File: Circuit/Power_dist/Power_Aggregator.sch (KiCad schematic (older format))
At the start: 8 parts, among them P16 XT60, P17 XT60, Q6 AUIRFS8409-7P, Q7 AUIRFS8409-7P, U5 LTC4357, U6 LTC4357

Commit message: edit sch and add pcix16
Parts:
- F6, F7: footprint Zeabus:FUSE_AUTO -> zeabus:FUSE_AUTO
- P16, P17: footprint Zeabus:XT60 -> zeabus:XT60
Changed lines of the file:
@@
 EESchema Schematic File Version 2
+LIBS:Power_Distributor-rescue
 LIBS:power
 LIBS:device
@@
 LIBS:zeabus
 LIBS:ftdi
+LIBS:Power_Distributor-cache
 EELAYER 25 0
 EELAYER END
@@
 F 0 "F7" H 4400 4050 50  0000 C CNN
 F 1 "FUSE" H 4200 3950 50  0000 C CNN
-F 2 "Zeabus:FUSE_AUTO" H 4300 4000 60  0001 C CNN
+F 2 "zeabus:FUSE_AUTO" H 4300 4000 60  0001 C CNN
 F 3 "" H 4300 4000 60  0000 C CNN
 	1    4300 4000
@@
 F 0 "P17" H 3850 4600 50  0000 C CNN
 F 1 "XT60" H 3850 4300 50  0000 C CNN
-F 2 "Zeabus:XT60" H 3850 4450 60  0001 C CNN
+F 2 "zeabus:XT60" H 3850 4450 60  0001 C CNN
 F 3 "" H 3850 4450 60  0000 C CNN
 	1    3850 4450
@@
 $EndComp
 $Comp
-L GND #PWR040
+L GND #PWR025
 U 1 1 5626F752
 P 6350 5250
-F 0 "#PWR040" H 6350 5000 50  0001 C CNN
+F 0 "#PWR025" H 6350 5000 50  0001 C CNN
 F 1 "GND" H 6350 5100 50  0000 C CNN
 F 2 "" H 6350 5250 60  0000 C CNN
@@
 $EndComp
 $Comp
-L GND #PWR041
+L GND #PWR026
 U 1 1 5626F76E
 P 4050 4600
-F 0 "#PWR041" H 4050 4350 50  0001 C CNN
+F 0 "#PWR026" H 4050 4350 50  0001 C CNN
 F 1 "GND" H 4050 4450 50  0000 C CNN
 F 2 "" H 4050 4600 60  0000 C CNN
@@
 F 0 "F6" H 4400 2150 50  0000 C CNN
 F 1 "FUSE" H 4200 2050 50  0000 C CNN
-F 2 "Zeabus:FUSE_AUTO" H 4300 2100 60  0001 C CNN
+F 2 "zeabus:FUSE_AUTO" H 4300 2100 60  0001 C CNN
 F 3 "" H 4300 2100 60  0000 C CNN
 	1    4300 2100
@@
 F 0 "P16" H 3850 2700 50  0000 C CNN
 F 1 "XT60" H 3850 2400 50  0000 C CNN
-F 2 "Zeabus:XT60" H 3850 2550 60  0001 C CNN
+F 2 "zeabus:XT60" H 3850 2550 60  0001 C CNN
 F 3 "" H 3850 2550 60  0000 C CNN
 	1    3850 2550
@@
 $EndComp
 $Comp
-L GND #PWR042
+L GND #PWR027
 U 1 1 5626F959
 P 6350 3350
-F 0 "#PWR042" H 6350 3100 50  0001 C CNN
+F 0 "#PWR027" H 6350 3100 50  0001 C CNN
 F 1 "GND" H 6350 3200 50  0000 C CNN
 F 2 "" H 6350 3350 60  0000 C CNN
@@
 $EndComp
 $Comp
-L GND #PWR043
+L GND #PWR028
 U 1 1 5626F95F
 P 4050 2700
-F 0 "#PWR043" H 4050 2450 50  0001 C CNN
+F 0 "#PWR028" H 4050 2450 50  0001 C CNN
 F 1 "GND" H 4050 2550 50  0000 C CNN
 F 2 "" H 4050 2700 60  0000 C CNN

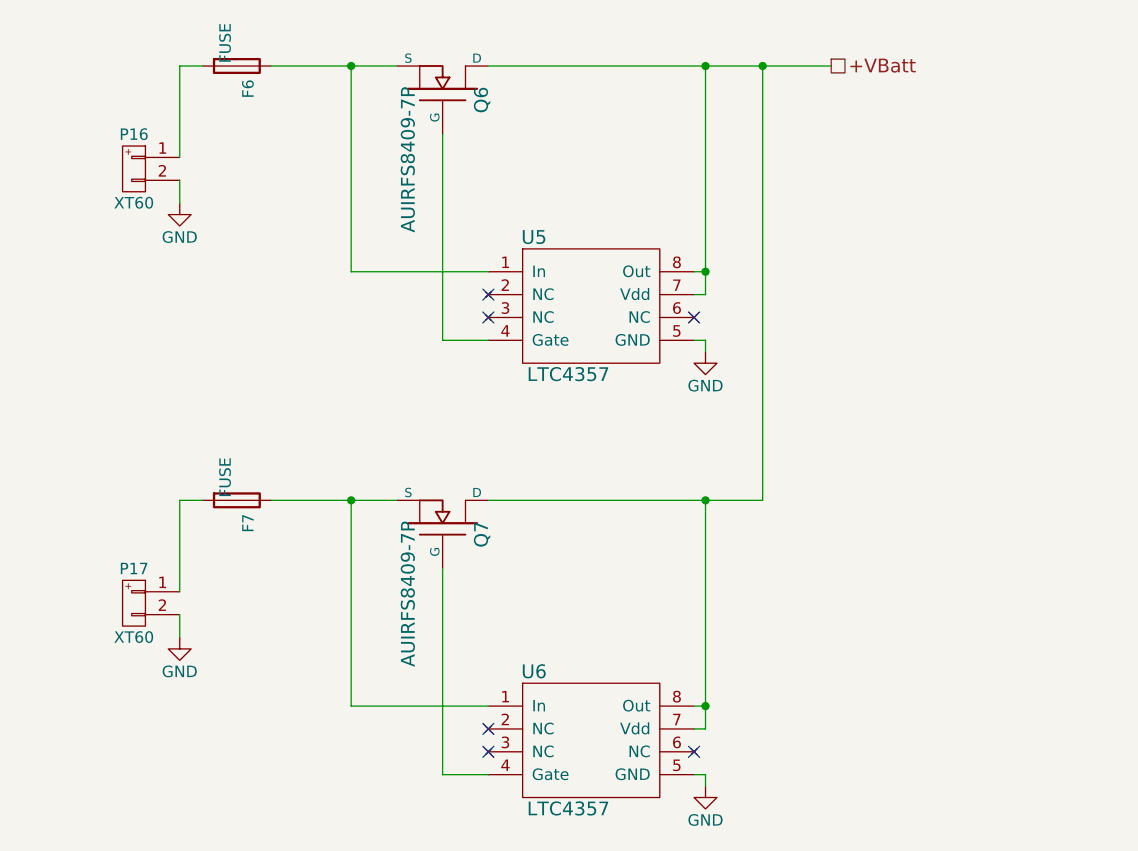
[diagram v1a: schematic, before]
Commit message: delete fuses at thrusters and oring + add power on jumper
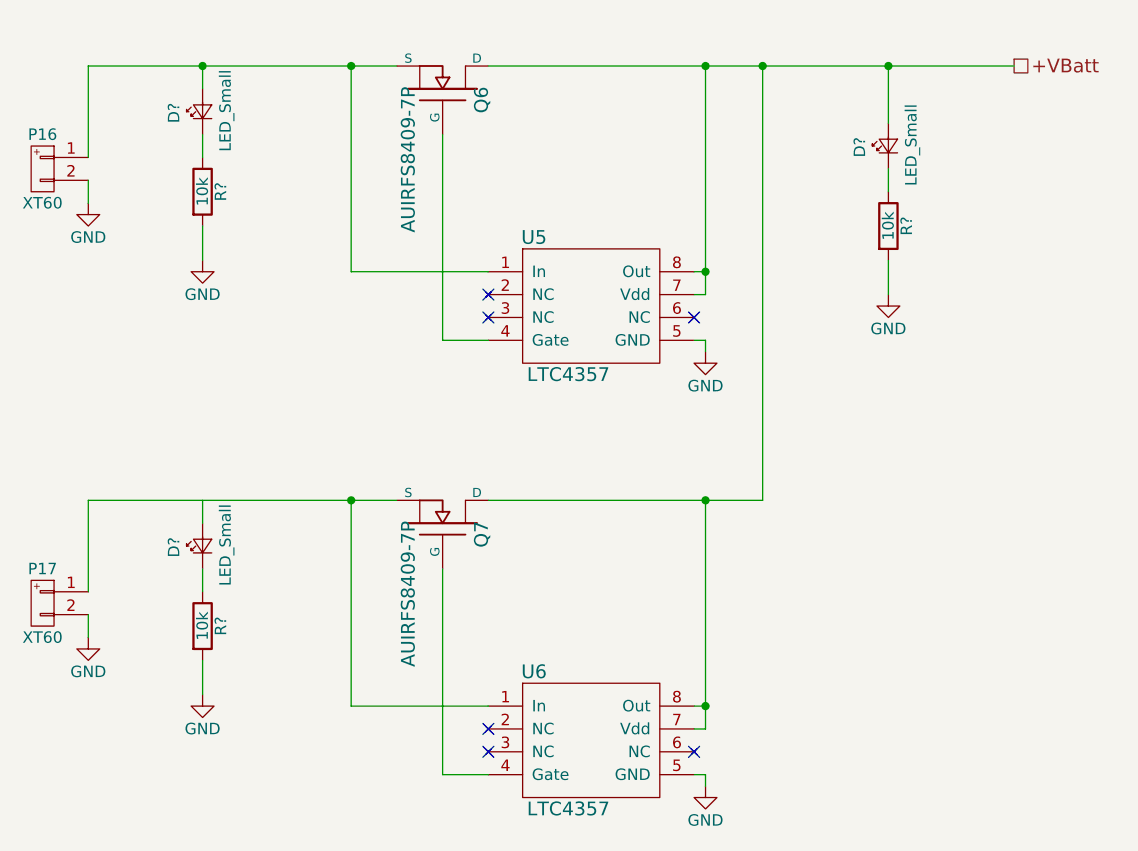
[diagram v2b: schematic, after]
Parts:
- removed F6, F7: FUSE, zeabus:FUSE_AUTO, symbol Fuse
- added D? (x3): LED_Small, LEDs:LED_0603, symbol LED_Small
- added R? (x3): 10k, Resistors_SMD:R_0603, symbol R
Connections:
- net +VBatt: now also D?.2 (A)
- net GND: now also R?.2, R?.2, R?.2
- net at Q7.S, U6.1 (In): now also P17.1 (P1)
- net at Q6.S, U5.1 (In): now also P16.1 (P1), D?.2 (A)
- new net: D?.1 (K), R?.1 (x3)
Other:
- moved on the sheet: P16, P17
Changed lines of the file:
@@
 $Descr A4 11693 8268
 encoding utf-8
-Sheet 8 9
+Sheet 6 8
 Title "Power Aggregator"
 Date "2017-04-06"
@@
 $EndDescr
 $Comp
-L Fuse F7
-U 1 1 5626464E
-P 4300 4000
-F 0 "F7" H 4400 4050 50  0000 C CNN
-F 1 "FUSE" H 4200 3950 50  0000 C CNN
-F 2 "zeabus:FUSE_AUTO" H 4300 4000 60  0001 C CNN
-F 3 "" H 4300 4000 60  0000 C CNN
-	1    4300 4000
-	0    1    1    0
-$EndComp
-$Comp
 L XT60 P17
 U 1 1 5626F4F4
-P 3850 4450
-F 0 "P17" H 3850 4600 50  0000 C CNN
-F 1 "XT60" H 3850 4300 50  0000 C CNN
-F 2 "zeabus:XT60" H 3850 4450 60  0001 C CNN
-F 3 "" H 3850 4450 60  0000 C CNN
-	1    3850 4450
+P 3450 4450
+F 0 "P17" H 3450 4600 50  0000 C CNN
+F 1 "XT60" H 3450 4300 50  0000 C CNN
+F 2 "zeabus:XT60" H 3450 4450 60  0001 C CNN
+F 3 "" H 3450 4450 60  0000 C CNN
+	1    3450 4450
 	-1   0    0    -1
 $EndComp
@@
 L GND #PWR026
 U 1 1 5626F76E
-P 4050 4600
-F 0 "#PWR026" H 4050 4350 50  0001 C CNN
-F 1 "GND" H 4050 4450 50  0000 C CNN
-F 2 "" H 4050 4600 60  0000 C CNN
-F 3 "" H 4050 4600 60  0000 C CNN
-	1    4050 4600
-	1    0    0    -1
-$EndComp
-Wire Wire Line
-	4050 4400 4050 4000
-Wire Wire Line
-	4450 4000 5000 4000
+P 3650 4600
+F 0 "#PWR026" H 3650 4350 50  0001 C CNN
+F 1 "GND" H 3650 4450 50  0000 C CNN
+F 2 "" H 3650 4600 60  0000 C CNN
+F 3 "" H 3650 4600 60  0000 C CNN
+	1    3650 4600
+	1    0    0    -1
+$EndComp
+Wire Wire Line
+	3650 4400 3650 4000
+Wire Wire Line
+	3650 4000 5000 4000
 Wire Wire Line
 	5400 5200 5200 5200
@@
 	6350 5200 6300 5200
 Wire Wire Line
-	4050 4500 4050 4600
-$Comp
-L Fuse F6
-U 1 1 5626F941
-P 4300 2100
-F 0 "F6" H 4400 2150 50  0000 C CNN
-F 1 "FUSE" H 4200 2050 50  0000 C CNN
-F 2 "zeabus:FUSE_AUTO" H 4300 2100 60  0001 C CNN
-F 3 "" H 4300 2100 60  0000 C CNN
-	1    4300 2100
-	0    1    1    0
-$EndComp
+	3650 4500 3650 4600
 $Comp
 L XT60 P16
 U 1 1 5626F947
-P 3850 2550
-F 0 "P16" H 3850 2700 50  0000 C CNN
-F 1 "XT60" H 3850 2400 50  0000 C CNN
-F 2 "zeabus:XT60" H 3850 2550 60  0001 C CNN
-F 3 "" H 3850 2550 60  0000 C CNN
-	1    3850 2550
+P 3450 2550
+F 0 "P16" H 3450 2700 50  0000 C CNN
+F 1 "XT60" H 3450 2400 50  0000 C CNN
+F 2 "zeabus:XT60" H 3450 2550 60  0001 C CNN
+F 3 "" H 3450 2550 60  0000 C CNN
+	1    3450 2550
 	-1   0    0    -1
 $EndComp
@@
 L GND #PWR028
 U 1 1 5626F95F
-P 4050 2700
-F 0 "#PWR028" H 4050 2450 50  0001 C CNN
-F 1 "GND" H 4050 2550 50  0000 C CNN
-F 2 "" H 4050 2700 60  0000 C CNN
-F 3 "" H 4050 2700 60  0000 C CNN
-	1    4050 2700
-	1    0    0    -1
-$EndComp
-Wire Wire Line
-	4050 2500 4050 2100
-Wire Wire Line
-	4450 2100 5000 2100
+P 3650 2700
+F 0 "#PWR028" H 3650 2450 50  0001 C CNN
+F 1 "GND" H 3650 2550 50  0000 C CNN
+F 2 "" H 3650 2700 60  0000 C CNN
+F 3 "" H 3650 2700 60  0000 C CNN
+	1    3650 2700
+	1    0    0    -1
+$EndComp
+Wire Wire Line
+	3650 2500 3650 2100
+Wire Wire Line
+	3650 2100 5000 2100
 Wire Wire Line
 	5400 3300 5200 3300
@@
 	6350 3000 6300 3000
 Wire Wire Line
-	5400 2100 6900 2100
+	5400 2100 7700 2100
 Connection ~ 6350 3000
 Wire Wire Line
@@
 	6350 3300 6300 3300
 Wire Wire Line
-	4050 2600 4050 2700
-Text HLabel 6900 2100 2    60   UnSpc ~ 0
+	3650 2600 3650 2700
+Text HLabel 7700 2100 2    60   UnSpc ~ 0
 +VBatt
 Connection ~ 6350 2100
@@
 Connection ~ 6600 2100
 Connection ~ 6350 4000
-Wire Wire Line
-	4050 2100 4150 2100
-Wire Wire Line
-	4050 4000 4150 4000
 NoConn ~ 6300 5100
 NoConn ~ 5400 5000
@@
 NoConn ~ 5400 3200
 NoConn ~ 6300 3200
+$Comp
+L LED_Small D?
+U 1 1 5A394E28
+P 4150 2300
+F 0 "D?" H 4100 2425 50  0000 L CNN
+F 1 "LED_Small" H 3975 2200 50  0000 L CNN
+F 2 "LEDs:LED_0603" V 4150 2300 50  0001 C CNN
+F 3 "" V 4150 2300 50  0001 C CNN
+	1    4150 2300
+	0    -1   -1   0
+$EndComp
+$Comp
+L R R?
+U 1 1 5A394EA7
+P 4150 2650
+F 0 "R?" V 4230 2650 50  0000 C CNN
+F 1 "10k" V 4150 2650 50  0000 C CNN
+F 2 "Resistors_SMD:R_0603" V 4080 2650 50  0001 C CNN
+F 3 "" H 4150 2650 50  0001 C CNN
+	1    4150 2650
+	1    0    0    -1
+$EndComp
+$Comp
+L GND #PWR?
+U 1 1 5A394FC4
+P 4150 2950
+F 0 "#PWR?" H 4150 2700 50  0001 C CNN
+F 1 "GND" H 4150 2800 50  0000 C CNN
+F 2 "" H 4150 2950 60  0000 C CNN
+F 3 "" H 4150 2950 60  0000 C CNN
+	1    4150 2950
+	1    0    0    -1
+$EndComp
+Wire Wire Line
+	4150 2200 4150 2100
+Connection ~ 4150 2100
+Wire Wire Line
+	4150 2400 4150 2500
+Wire Wire Line
+	4150 2800 4150 2950
+$Comp
+L LED_Small D?
+U 1 1 5A3951EC
+P 4150 4200
+F 0 "D?" H 4100 4325 50  0000 L CNN
+F 1 "LED_Small" H 3975 4100 50  0000 L CNN
+F 2 "LEDs:LED_0603" V 4150 4200 50  0001 C CNN
+F 3 "" V 4150 4200 50  0001 C CNN
+	1    4150 4200
+	0    -1   -1   0
+$EndComp
+$Comp
+L R R?
+U 1 1 5A3951F2
+P 4150 4550
+F 0 "R?" V 4230 4550 50  0000 C CNN
+F 1 "10k" V 4150 4550 50  0000 C CNN
+F 2 "Resistors_SMD:R_0603" V 4080 4550 50  0001 C CNN
+F 3 "" H 4150 4550 50  0001 C CNN
+	1    4150 4550
+	1    0    0    -1
+$EndComp
+$Comp
+L GND #PWR?
+U 1 1 5A3951F8
+P 4150 4850
+F 0 "#PWR?" H 4150 4600 50  0001 C CNN
+F 1 "GND" H 4150 4700 50  0000 C CNN
+F 2 "" H 4150 4850 60  0000 C CNN
+F 3 "" H 4150 4850 60  0000 C CNN
+	1    4150 4850
+	1    0    0    -1
+$EndComp
+Wire Wire Line
+	4150 4100 4150 4000
+Wire Wire Line
+	4150 4300 4150 4400
+Wire Wire Line
+	4150 4700 4150 4850
+$Comp
+L LED_Small D?
+U 1 1 5A397232
+P 7150 2450
+F 0 "D?" H 7100 2575 50  0000 L CNN
+F 1 "LED_Small" H 6975 2350 50  0000 L CNN
+F 2 "LEDs:LED_0603" V 7150 2450 50  0001 C CNN
+F 3 "" V 7150 2450 50  0001 C CNN
+	1    7150 2450
+	0    -1   -1   0
+$EndComp
+$Comp
+L R R?
+U 1 1 5A397238
+P 7150 2800
+F 0 "R?" V 7230 2800 50  0000 C CNN
+F 1 "10k" V 7150 2800 50  0000 C CNN
+F 2 "Resistors_SMD:R_0603" V 7080 2800 50  0001 C CNN
+F 3 "" H 7150 2800 50  0001 C CNN
+	1    7150 2800
+	1    0    0    -1
+$EndComp
+$Comp
+L GND #PWR?
+U 1 1 5A39723E
+P 7150 3100
+F 0 "#PWR?" H 7150 2850 50  0001 C CNN
+F 1 "GND" H 7150 2950 50  0000 C CNN
+F 2 "" H 7150 3100 60  0000 C CNN
+F 3 "" H 7150 3100 60  0000 C CNN
+	1    7150 3100
+	1    0    0    -1
+$EndComp
+Wire Wire Line
+	7150 2100 7150 2350
+Wire Wire Line
+	7150 2550 7150 2650
+Wire Wire Line
+	7150 2950 7150 3100
+Connection ~ 7150 2100
 $EndSCHEMATC

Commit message: component alignment on pcb
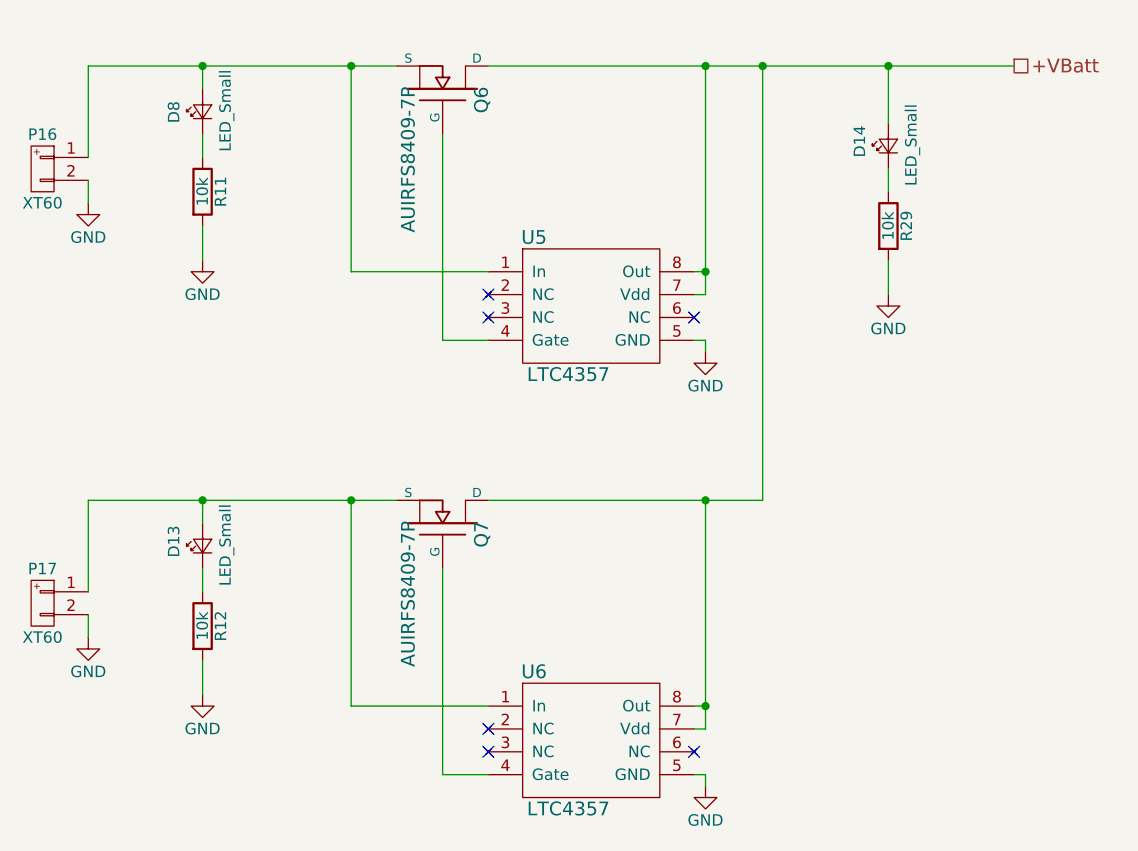
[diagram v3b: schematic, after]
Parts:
- D13, D14, D8: renamed from D?; footprint LEDs:LED_0603 -> LEDs:LED_0603_HandSoldering
- R11, R12, R29: renamed from R?; footprint Resistors_SMD:R_0603 -> Resistors_SMD:R_0603_HandSoldering
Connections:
- net at P17.1 (P1), Q7.S, U6.1 (In): now also D13.2 (A)
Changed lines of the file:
@@
 $EndComp
 $Comp
-L GND #PWR025
+L GND #PWR030
 U 1 1 5626F752
 P 6350 5250
-F 0 "#PWR025" H 6350 5000 50  0001 C CNN
+F 0 "#PWR030" H 6350 5000 50  0001 C CNN
 F 1 "GND" H 6350 5100 50  0000 C CNN
 F 2 "" H 6350 5250 60  0000 C CNN
@@
 $EndComp
 $Comp
-L GND #PWR026
+L GND #PWR031
 U 1 1 5626F76E
 P 3650 4600
-F 0 "#PWR026" H 3650 4350 50  0001 C CNN
+F 0 "#PWR031" H 3650 4350 50  0001 C CNN
 F 1 "GND" H 3650 4450 50  0000 C CNN
 F 2 "" H 3650 4600 60  0000 C CNN
@@
 $EndComp
 $Comp
-L GND #PWR027
+L GND #PWR032
 U 1 1 5626F959
 P 6350 3350
-F 0 "#PWR027" H 6350 3100 50  0001 C CNN
+F 0 "#PWR032" H 6350 3100 50  0001 C CNN
 F 1 "GND" H 6350 3200 50  0000 C CNN
 F 2 "" H 6350 3350 60  0000 C CNN
@@
 $EndComp
 $Comp
-L GND #PWR028
+L GND #PWR033
 U 1 1 5626F95F
 P 3650 2700
-F 0 "#PWR028" H 3650 2450 50  0001 C CNN
+F 0 "#PWR033" H 3650 2450 50  0001 C CNN
 F 1 "GND" H 3650 2550 50  0000 C CNN
 F 2 "" H 3650 2700 60  0000 C CNN
@@
 NoConn ~ 6300 3200
 $Comp
-L LED_Small D?
+L LED_Small D8
 U 1 1 5A394E28
 P 4150 2300
-F 0 "D?" H 4100 2425 50  0000 L CNN
+F 0 "D8" H 4100 2425 50  0000 L CNN
 F 1 "LED_Small" H 3975 2200 50  0000 L CNN
-F 2 "LEDs:LED_0603" V 4150 2300 50  0001 C CNN
+F 2 "LEDs:LED_0603_HandSoldering" V 4150 2300 50  0001 C CNN
 F 3 "" V 4150 2300 50  0001 C CNN
 	1    4150 2300
@@
 $EndComp
 $Comp
-L R R?
+L R R11
 U 1 1 5A394EA7
 P 4150 2650
-F 0 "R?" V 4230 2650 50  0000 C CNN
+F 0 "R11" V 4230 2650 50  0000 C CNN
 F 1 "10k" V 4150 2650 50  0000 C CNN
-F 2 "Resistors_SMD:R_0603" V 4080 2650 50  0001 C CNN
+F 2 "Resistors_SMD:R_0603_HandSoldering" V 4080 2650 50  0001 C CNN
 F 3 "" H 4150 2650 50  0001 C CNN
 	1    4150 2650
@@
 $EndComp
 $Comp
-L GND #PWR?
+L GND #PWR034
 U 1 1 5A394FC4
 P 4150 2950
-F 0 "#PWR?" H 4150 2700 50  0001 C CNN
+F 0 "#PWR034" H 4150 2700 50  0001 C CNN
 F 1 "GND" H 4150 2800 50  0000 C CNN
 F 2 "" H 4150 2950 60  0000 C CNN
@@
 	4150 2800 4150 2950
 $Comp
-L LED_Small D?
+L LED_Small D13
 U 1 1 5A3951EC
 P 4150 4200
-F 0 "D?" H 4100 4325 50  0000 L CNN
+F 0 "D13" H 4100 4325 50  0000 L CNN
 F 1 "LED_Small" H 3975 4100 50  0000 L CNN
-F 2 "LEDs:LED_0603" V 4150 4200 50  0001 C CNN
+F 2 "LEDs:LED_0603_HandSoldering" V 4150 4200 50  0001 C CNN
 F 3 "" V 4150 4200 50  0001 C CNN
 	1    4150 4200
@@
 $EndComp
 $Comp
-L R R?
+L R R12
 U 1 1 5A3951F2
 P 4150 4550
-F 0 "R?" V 4230 4550 50  0000 C CNN
+F 0 "R12" V 4230 4550 50  0000 C CNN
 F 1 "10k" V 4150 4550 50  0000 C CNN
-F 2 "Resistors_SMD:R_0603" V 4080 4550 50  0001 C CNN
+F 2 "Resistors_SMD:R_0603_HandSoldering" V 4080 4550 50  0001 C CNN
 F 3 "" H 4150 4550 50  0001 C CNN
 	1    4150 4550
@@
 $EndComp
 $Comp
-L GND #PWR?
+L GND #PWR035
 U 1 1 5A3951F8
 P 4150 4850
-F 0 "#PWR?" H 4150 4600 50  0001 C CNN
+F 0 "#PWR035" H 4150 4600 50  0001 C CNN
 F 1 "GND" H 4150 4700 50  0000 C CNN
 F 2 "" H 4150 4850 60  0000 C CNN
@@
 $EndComp
 Wire Wire Line
-	4150 4100 4150 4000
-Wire Wire Line
 	4150 4300 4150 4400
 Wire Wire Line
 	4150 4700 4150 4850
 $Comp
-L LED_Small D?
+L LED_Small D14
 U 1 1 5A397232
 P 7150 2450
-F 0 "D?" H 7100 2575 50  0000 L CNN
+F 0 "D14" H 7100 2575 50  0000 L CNN
 F 1 "LED_Small" H 6975 2350 50  0000 L CNN
-F 2 "LEDs:LED_0603" V 7150 2450 50  0001 C CNN
+F 2 "LEDs:LED_0603_HandSoldering" V 7150 2450 50  0001 C CNN
 F 3 "" V 7150 2450 50  0001 C CNN
 	1    7150 2450
@@
 $EndComp
 $Comp
-L R R?
+L R R29
 U 1 1 5A397238
 P 7150 2800
-F 0 "R?" V 7230 2800 50  0000 C CNN
+F 0 "R29" V 7230 2800 50  0000 C CNN
 F 1 "10k" V 7150 2800 50  0000 C CNN
-F 2 "Resistors_SMD:R_0603" V 7080 2800 50  0001 C CNN
+F 2 "Resistors_SMD:R_0603_HandSoldering" V 7080 2800 50  0001 C CNN
 F 3 "" H 7150 2800 50  0001 C CNN
 	1    7150 2800
@@
 $EndComp
 $Comp
-L GND #PWR?
+L GND #PWR036
 U 1 1 5A39723E
 P 7150 3100
-F 0 "#PWR?" H 7150 2850 50  0001 C CNN
+F 0 "#PWR036" H 7150 2850 50  0001 C CNN
 F 1 "GND" H 7150 2950 50  0000 C CNN
 F 2 "" H 7150 3100 60  0000 C CNN
@@
 	7150 2950 7150 3100
 Connection ~ 7150 2100
+Wire Wire Line
+	4150 4100 4150 4000
+Connection ~ 4150 4000
 $EndSCHEMATC
